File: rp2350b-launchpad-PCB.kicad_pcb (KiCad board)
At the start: 2 copper layers, 58.4 x 83.8 mm, 126 parts, among them J1 Target Isolation Jumpers, J10 PWR Header, J11 LP Extension Heder, J12 LP Header right, J13 PWR Header, J2 Jumper, J3 LiPo 3,7V Batt., J4 Jumper, J5 DBG_PRGM, J6 UART_DBG, J7 DGB Exp. Header, J8 Jumper, J9 LP Header left, SW1 Switch_SP3T, SW2 RESET, SW3 BOOT, U1 MCP73831, U10 WS2812B-2020, U11 WS2812B-2020, U12 WS2812B-2020, U13 WS2812B-2020, U14 WS2812B-2020, U15 WS2812B-2020, U16 WS2812B-2020, U2 XC9142B50C, U3 XC6220B33, U4 25Q32, U5 RP2040, U6 25Q64, U7 APS6404L-3SQR, U8 RP2350_80QFN, U9 WS2812B-2020, Y1 12MHz, Y2 12MHz

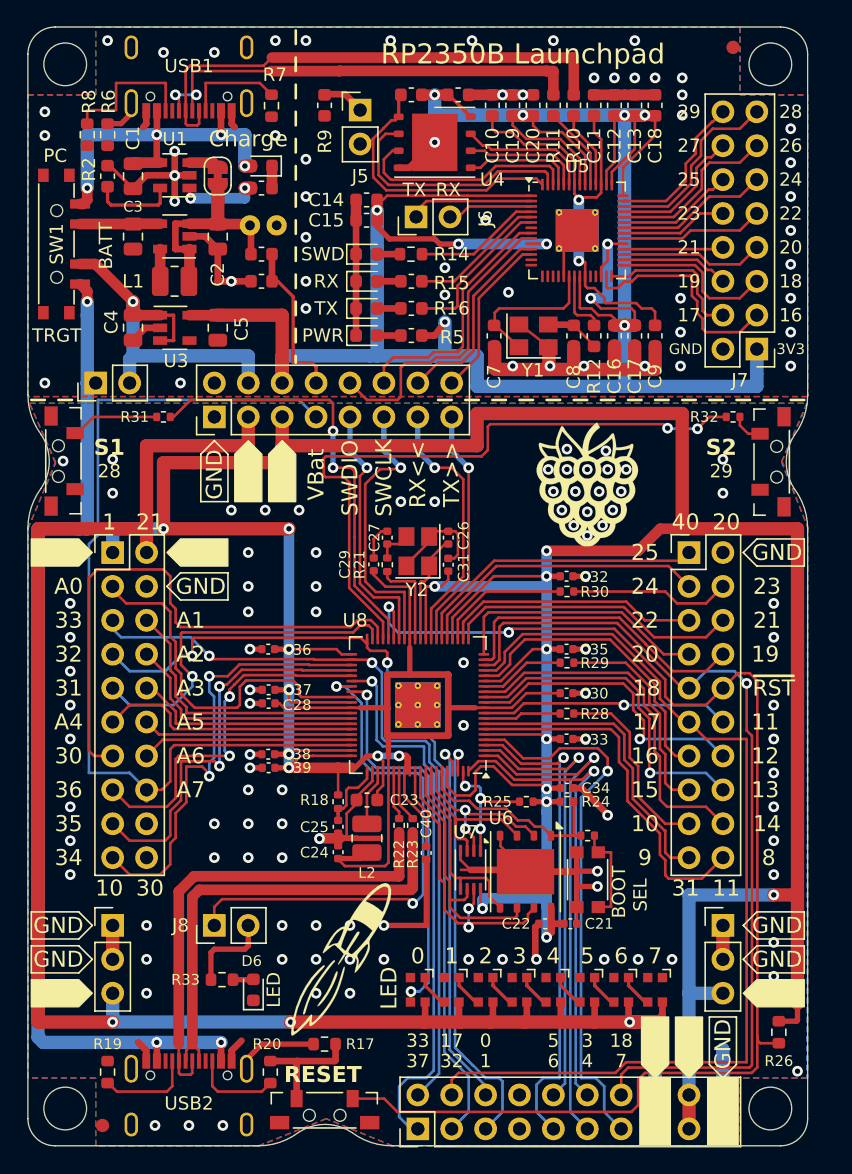
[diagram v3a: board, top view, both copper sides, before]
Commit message: Ready for Version v1.0. Changed PCB to comply with RPi design 'rules'. Without using special components and PCB designs, the PCB may not be produced :\
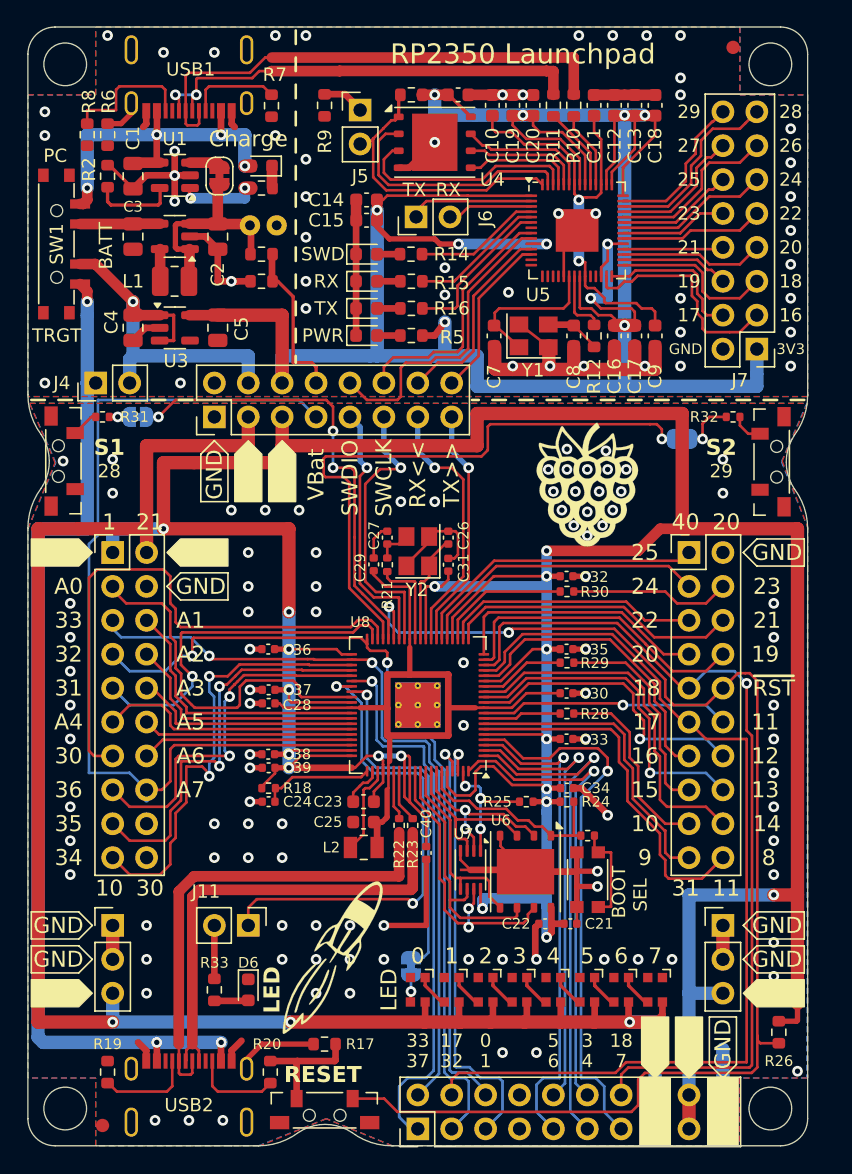
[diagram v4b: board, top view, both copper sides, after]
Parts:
- added J10: Jumper, Jumper:SolderJumper-2_P1.3mm_Bridged_RoundedPad1.0x1.5mm, B.Cu at (159.5, 98.2)
- added J8: Jumper, Jumper:SolderJumper-2_P1.3mm_Bridged_RoundedPad1.0x1.5mm, B.Cu at (139.2, 137.7)
- added J9: Jumper, Jumper:SolderJumper-2_P1.3mm_Bridged_RoundedPad1.0x1.5mm, B.Cu at (118.7, 96.5)
- C25: footprint Capacitor_SMD:C_0402_1005Metric -> Capacitor_SMD:C_0603_1608Metric
- C26, C27, C7, C8: value 22pF -> 15pF
- G***: moved to F.Cu
- G***: moved to B.Cu
- L2: value 4u7 -> 3u3; footprint Inductor_SMD:L_1008_2520Metric -> rp2350b-launchpad-PCB:AOTA-B201610S3R3-101-T
- U5: footprint Package_DFN_QFN:QFN-56-1EP_7x7mm_P0.4mm_EP3.2x3.2mm_ThermalVias -> Package_DFN_QFN:QFN-56-1EP_7x7mm_P0.4mm_EP3.2x3.2mm
- USB1, USB2: footprint rp2350b-launchpad-PCB:USB-C-GCT-USB4105 -> rp2350b-launchpad-PCB:GT-USB-7010B
- moved G*** 44.1 mm to (135.6, 96.7), turned to 90 degrees
- moved G*** 21.2 mm to (152.4, 101.6)
- moved G*** 9.93 mm to (146.0, 139.3), turned to 0 degrees
- moved C24 5.54 mm to (128.5, 125.3), turned to 180 degrees
- moved R18 5.31 mm to (128.5, 124.3), turned to 180 degrees
- moved R31 4.57 mm to (116.1, 96.5)
- moved C25 2.95 mm to (135.6, 126.9), turned to 0 degrees
- moved J11 2.55 mm to (127.0, 134.6), turned to -90 degrees
- moved R33 0.95 mm to (124.5, 139.4), turned to -90 degrees
- moved L2 0.73 mm to (135.7, 128.8), turned to 180 degrees
- moved D6 0.38 mm to (127.0, 139.4), turned to -90 degrees
- moved C23 0.28 mm to (135.6, 125.3)
- moved J2 0.13 mm to (124.8, 78.5)
- renumbered J8 to J11, J9 to J12, J10 to J13, J11 to J14, J12 to J15, J13 to J16
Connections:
- R31 pad 1: Net-(U8-GPIO28) -> Net-(J9-Pad2)
- R32 pad 1: Net-(U8-GPIO29) -> Net-(J10-Pad2)
- U9 pad 3: Net-(U8-GPIO39) -> Net-(U9-DIN)
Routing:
- net +1V1: track 69.2 -> 55.2 mm
- net GND: track 93.1 -> 83.2 mm
- net GND_DBG: track 81.2 -> 76.7 mm, vias 52 -> 48
- net Net-(S1-B): track 6.61 -> 2.25 mm
- net Net-(J10-Pad2): track 0.00 -> 4.02 mm, vias 0 -> 1
- net Net-(U8-GPIO29): track 49.0 -> 45.4 mm, vias 2 -> 1
- net Net-(U8-GPIO39): track 29.0 -> 25.8 mm, vias 2 -> 1
- net Net-(U8-VREG_AVDD): track 5.23 -> 8.38 mm
- net Net-(U8-GPIO38): track 39.8 -> 36.8 mm
- net +3V3: track 317.6 -> 320.2 mm
- net Net-(U8-VREG_LX): track 4.28 -> 6.76 mm
- net Net-(J11-Pad2): track 6.56 -> 4.36 mm
- net Net-(U9-DIN): track 0.00 -> 2.04 mm, vias 0 -> 1
- net Net-(U8-GPIO28): track 33.0 -> 34.6 mm, vias 2 -> 3
- net Net-(J9-Pad2): track 0.00 -> 1.49 mm, vias 0 -> 1
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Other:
- board text added: "RP2350 Launchpad"
- board text added: "RP2350 Launchpad v1.0 © 2025 A. Terstegge"
- board text removed: "RP2350B Launchpad"
- board text removed: "RP2350B Launchpad v1.0 © A. Terstegge"

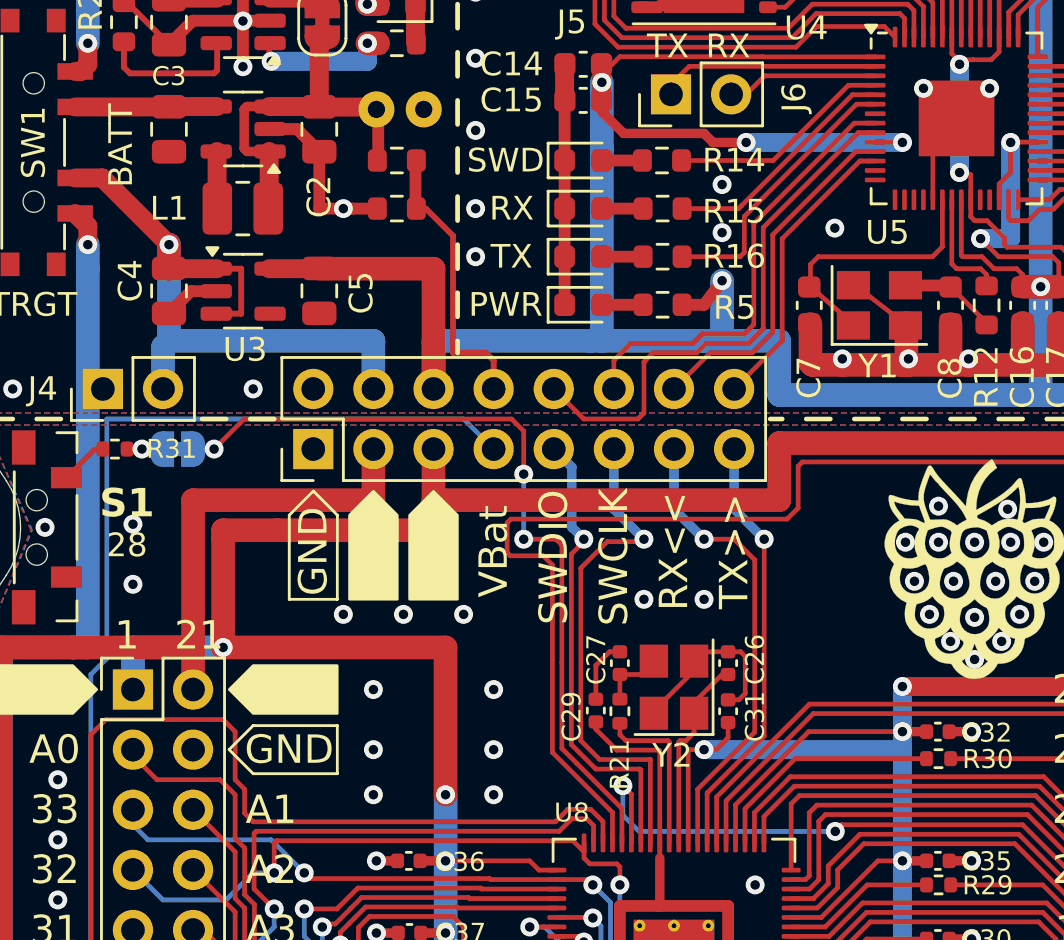
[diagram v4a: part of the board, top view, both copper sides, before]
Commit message: Updates for better JLCPCB processing. Version is now 1.1
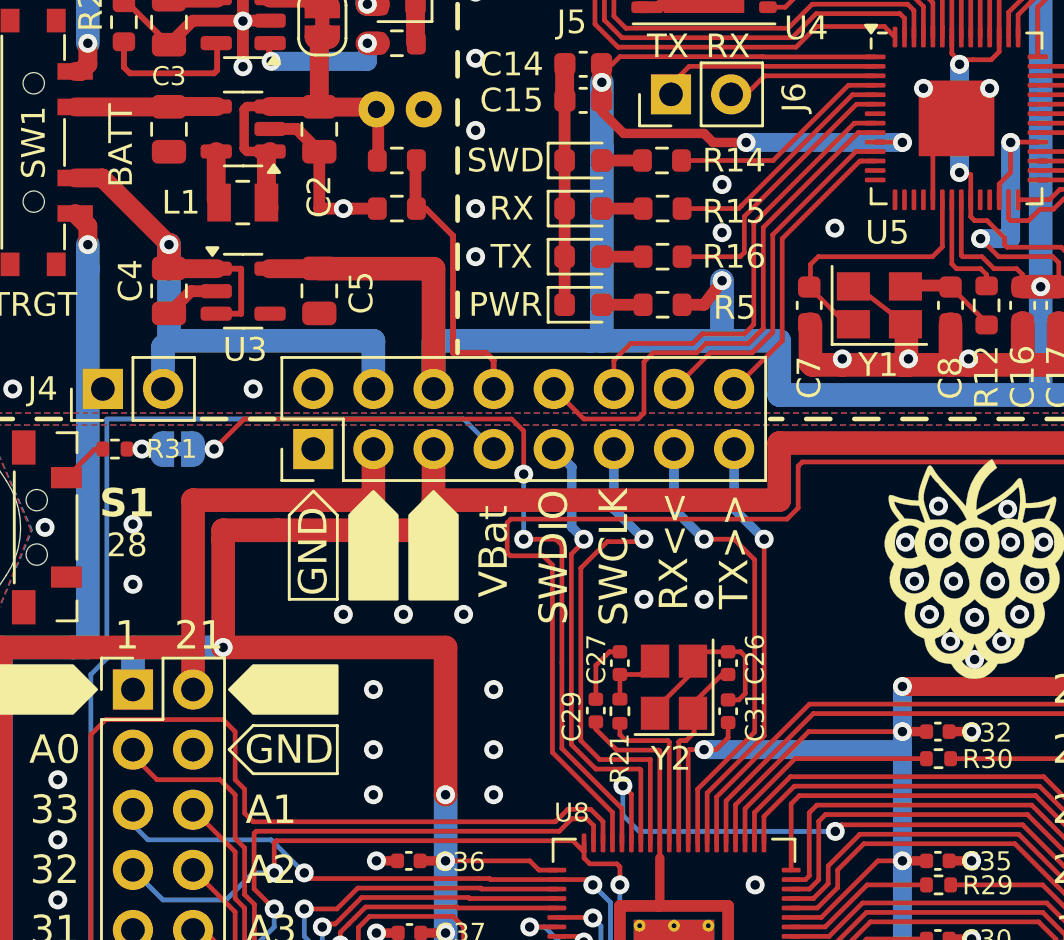
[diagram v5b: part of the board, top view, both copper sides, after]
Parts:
- C21: value 4,7u -> 4u7
- C23, C24, C25, C29: value 4.7u -> 4u7
- D3: value BLUE -> LED BLUE
- D4: value GREEN -> LED GREEN
- D5: value RED -> LED RED
- L1: footprint Inductor_SMD:L_1008_2520Metric -> rp2350b-launchpad-PCB:AOTA-B201610S3R3-101-T
- L2: value 3u3 -> 4u7
- SW1: value Switch_SP3T -> Power Select
- USB1, USB2: value USB-C-Socket -> USB-C Connector
- Y1, Y2: footprint Crystal:Crystal_SMD_TXC_7M-4Pin_3.2x2.5mm -> Crystal:Crystal_SMD_Abracon_ABM8AIG-4Pin_3.2x2.5mm
- moved L1 0.25 mm to (121.5, 86.1)
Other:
- board text added: "RP2350 Launchpad v1.1 © 2025 A. Terstegge"
- board text removed: "RP2350 Launchpad v1.0 © 2025 A. Terstegge"

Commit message: Ready for v1.1
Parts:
- C28, C30: value 100n -> 100nF
- J2: footprint Jumper:SolderJumper-2_P1.3mm_Bridged_RoundedPad1.0x1.5mm -> Jumper:SolderJumper-2_P1.3mm_Open_RoundedPad1.0x1.5mm
- moved J11 2.54 mm to (124.5, 134.6), turned to 0 degrees
- moved G*** 0.81 mm to (146.5, 138.6)
- moved C33 0.76 mm to (150.8, 119.9)
- moved D6 0.56 mm to (127.5, 139.2)
- moved R33 0.52 mm to (124.6, 140.0), turned to 0 degrees
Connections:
- J15 pad 19: /Target/GPIO9 -> /Target/GPIO2
- J15 pad 20: /Target/GPIO8 -> /Target/GPIO1
- U8 pad 6: /Target/GPIO8 -> /Target/I2C0_SDA
- U8 pad 7: /Target/GPIO9 -> /Target/I2C0_SCL
- U8 pad 77: /Target/I2C0_SDA -> /Target/~{RAM_CS}
- U8 pad 78: /Target/I2C0_SCL -> /Target/GPIO1
- U8 pad 79: /Target/~{RAM_CS} -> /Target/GPIO2
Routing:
- net /Target/GPIO1: track 0.00 -> 27.3 mm
- net /Target/GPIO8: track 27.2 -> 0.00 mm
- net /Target/GPIO9: track 22.9 -> 0.00 mm
- net /Target/GPIO2: track 0.00 -> 22.3 mm
- net /Target/~{RAM_CS}: track 10.4 -> 14.5 mm
- net +3V3: track 320.2 -> 317.1 mm
- net /Target/I2C0_SCL: track 32.9 -> 35.8 mm
- net Net-(U8-GPIO38): track 36.8 -> 39.4 mm
- net /Target/I2C0_SDA: track 28.9 -> 31.3 mm
- net Net-(J11-Pad2): track 4.36 -> 3.08 mm
- net GND: track 83.2 -> 84.1 mm
- net Net-(R23-Pad2): track 35.0 -> 35.5 mm
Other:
- board text added: "38"
- board text added: "39"
- board text added: "JLCJLCJLCJLC"
- board text added: "RGB"
- board text added: "RP2350"

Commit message: Last small fixes for v1.11
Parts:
- R1, R5: value 1k -> 2k
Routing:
- net /Target/~{RESET}: track 100.3 -> 98.5 mm
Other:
- board text added: "RP2350 Launchpad v1.11 © 2025 A. Terstegge"
- board text removed: "RP2350 Launchpad v1.1 © 2025 A. Terstegge"
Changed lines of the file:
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@@
 			)
 		)
-		(property "Value" "1k"
+		(property "Value" "2k"
 			(at 0 1.43 0)
 			(layer "F.Fab")
@@
 			)
 		)
-		(property "Datasheet" "https://jlcpcb.com/partdetail/21904-0603WAF1001T5E/C21190"
+		(property "Datasheet" "https://jlcpcb.com/partdetail/23702-0603WAF2001T5E/C22975"
 			(at 0 0 180)
 			(layer "F.Fab")
@@
 			)
 		)
-		(property "JLCPCB Part #" "C21190"
+		(property "JLCPCB Part #" "C22975"
 			(at 0 0 180)
 			(unlocked yes)
@@
 			)
 		)
-		(property "Value" "1k"
+		(property "Value" "2k"
 			(at 0 1.43 0)
 			(layer "F.Fab")
@@
 			)
 		)
-		(property "Datasheet" "https://jlcpcb.com/partdetail/21904-0603WAF1001T5E/C21190"
+		(property "Datasheet" "https://jlcpcb.com/partdetail/23702-0603WAF2001T5E/C22975"
 			(at 0 0 180)
 			(layer "F.Fab")
@@
 			)
 		)
-		(property "JLCPCB Part #" "C21190"
+		(property "JLCPCB Part #" "C22975"
 			(at 0 0 180)
 			(unlocked yes)
@@
 	)
 	(gr_text "JLCJLCJLCJLC"
-		(at 140.335 129.187 0)
+		(at 138.303 129.667 0)
 		(layer "B.SilkS")
 		(effects
@@
 	)
 	(gr_text "38"
-		(at 129.159 136.017 90)
+		(at 127.635 136.779 0)
 		(layer "F.SilkS")
 		(effects
@@
 	)
 	(gr_text "LED"
-		(at 127.508 136.017 90)
+		(at 127.762 135.255 0)
 		(layer "F.SilkS")
 		(effects
@@
 		)
 	)
-	(gr_text "RP2350 Launchpad v1.1\n© 2025 A. Terstegge"
+	(gr_text "RP2350 Launchpad v1.11\n© 2025 A. Terstegge"
 		(at 150.622 70.358 0)
 		(layer "Eco2.User")
@@
 	)
 	(segment
+		(start 165.138 117.729)
+		(end 165.138 121.666)
+		(width 0.2)
+		(layer "F.Cu")
+		(net 47)
+	)
+	(segment
 		(start 155.702 148.59)
 		(end 138.176 148.59)
@@
 	)
 	(segment
-		(start 161.29 118.11)
-		(end 158.877 118.11)
+		(start 164.249 116.84)
+		(end 165.138 117.729)
 		(width 0.2)
 		(layer "F.Cu")
@@
 	)
 	(segment
-		(start 137.9 111.103)
-		(end 137.541 110.744)
+		(start 161.29 118.11)
+		(end 158.877 118.11)
 		(width 0.2)
 		(layer "F.Cu")
@@
 	)
 	(segment
-		(start 165.138 116.29445)
-		(end 165.138 121.666)
+		(start 137.9 111.103)
+		(end 137.541 110.744)
 		(width 0.2)
 		(layer "F.Cu")
@@
 	)
 	(segment
-		(start 162.56 116.84)
-		(end 163.6776 115.7224)
-		(width 0.2)
-		(layer "F.Cu")
-		(net 47)
-	)
-	(segment
 		(start 165.138 142.875)
 		(end 165.138 143.002)
@@
 	)
 	(segment
-		(start 164.56595 115.7224)
-		(end 165.138 116.29445)
-		(width 0.2)
-		(layer "F.Cu")
-		(net 47)
-	)
-	(segment
 		(start 165.138 143.002)
 		(end 165.138 145.25)
@@
 	)
 	(segment
-		(start 163.6776 115.7224)
-		(end 164.2364 115.7224)
-		(width 0.2)
-		(layer "F.Cu")
-		(net 47)
-	)
-	(segment
 		(start 137.9 113.16)
 		(end 137.9 111.103)
@@
 	)
 	(segment
+		(start 162.56 116.84)
+		(end 164.249 116.84)
+		(width 0.2)
+		(layer "F.Cu")
+		(net 47)
+	)
+	(segment
 		(start 165.138 143.002)
 		(end 165.138 143.218)
@@
 	)
 	(segment
-		(start 164.2364 115.7224)
-		(end 164.56595 115.7224)
-		(width 0.2)
-		(layer "F.Cu")
-		(net 47)
-	)
-	(segment
 		(start 166.751 143.446)
 		(end 165.366 143.446)
@@
 	)
 	(segment
-		(start 164.338 116.4844)
-		(end 164.338 120.015)
-		(width 0.2)
-		(layer "F.Cu")
-		(net 70)
-	)
-	(segment
 		(start 154.635 111.963)
 		(end 146.101 111.963)
@@
 		(net 70)
 	)
+	(segment
+		(start 164.338 120.015)
+		(end 164.338 118.11)
+		(width 0.2)
+		(layer "F.Cu")
+		(net 70)
+	)
 	(via
-		(at 164.338 116.4844)
+		(at 164.338 118.11)
 		(size 0.8)
 		(drill 0.4)
@@
 		(width 0.2)
 		(layer "B.Cu")
+		(net 70)
+	)
+	(segment
+		(start 164.338 118.11)
+		(end 164.338 116.4844)
+		(width 0.2)
+		(layer "B.Cu")
